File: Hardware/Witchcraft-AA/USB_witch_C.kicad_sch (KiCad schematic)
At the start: 11 parts, among them J0 USB_C_Molex_201267-0005, J1 USB_C_Molex_201267-0005, U1 Z1 extreme

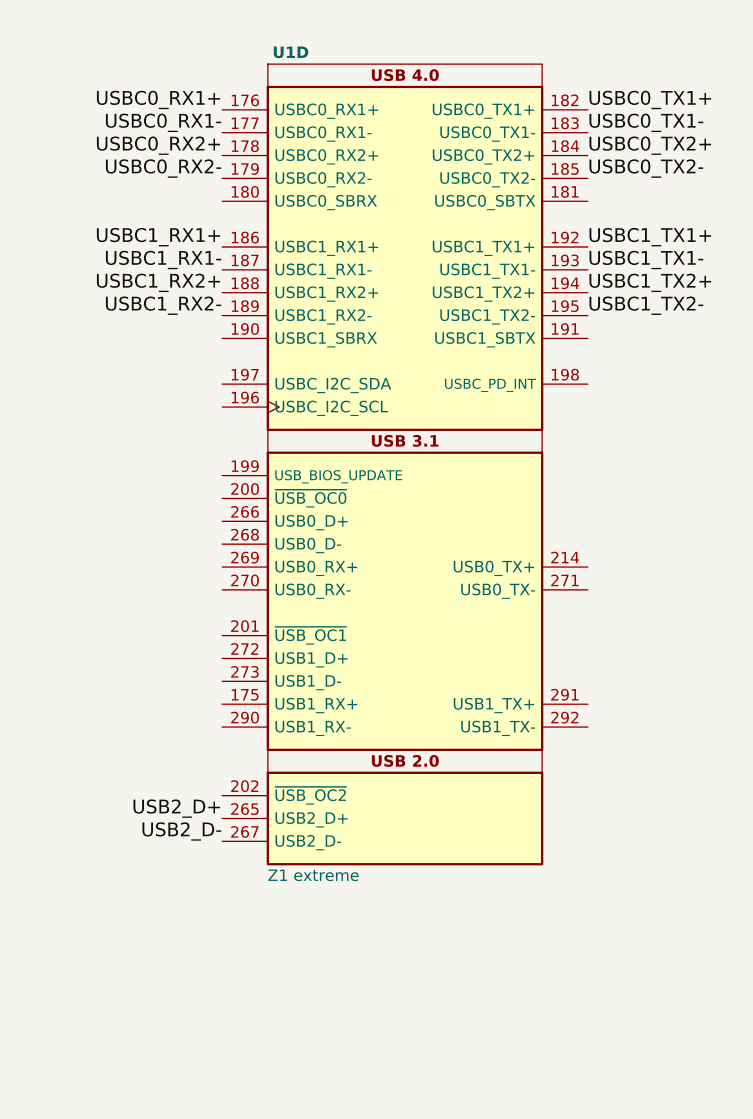
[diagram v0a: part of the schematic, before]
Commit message: ECAD: replaced the Z1 Extreme with the 7840U chip, as the AI-engine will be more useful for makers and non-gamers. MCAD: continued converting the outer shell towards a Assembly4-architecture, adding more items. Started a big change in design wherein I'm splitting the shell-design into a modular one, to accomodate removable controllers. Made some minor tweaks to the cooling-assembly, to accomodate the new, split shell-design. Updated the Readme to describe the project.
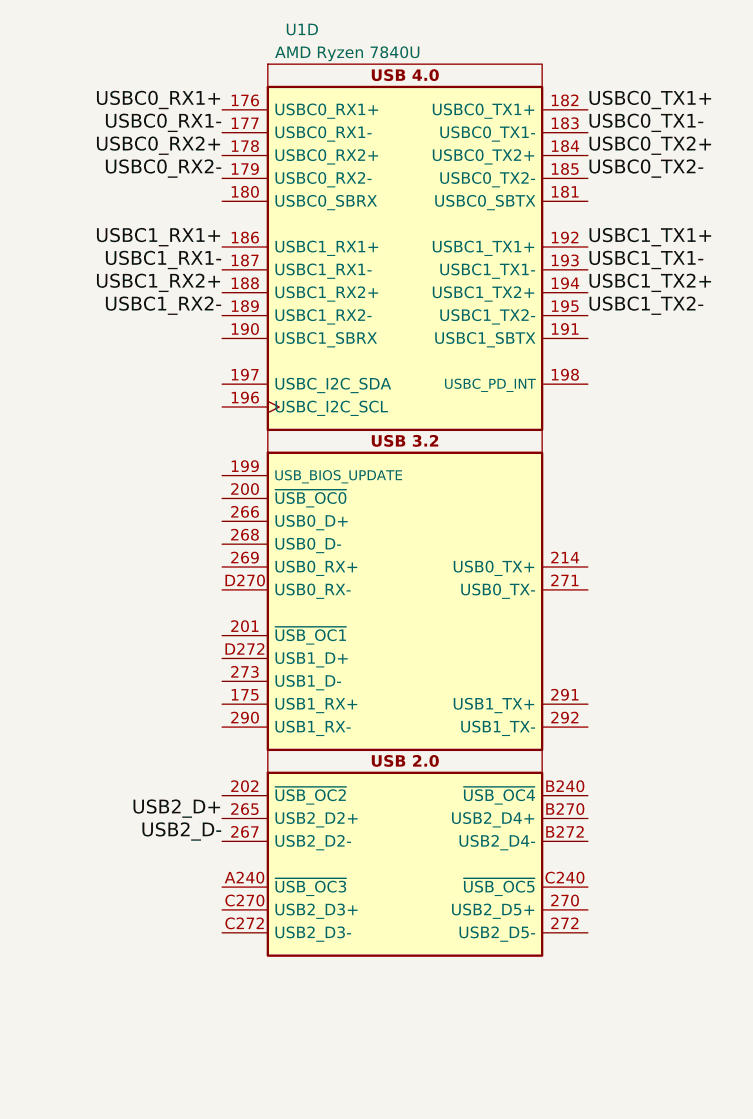
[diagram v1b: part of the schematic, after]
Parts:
- U1: value Z1 extreme -> AMD Ryzen 7840U; symbol LRJ-parts:AMD_Z1_extreme -> LRJ-parts:AMD_Ryzen_7840U_FP8; Details https://en.wikichip.org/wiki/amd/packages/socket_am5#Packag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 -> https://en.wikichip.org/wiki/amd/packages/fp6; Operating temperature (none) -> 0 C ~ 45 C
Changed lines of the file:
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@@
     )
   )
-  (symbol (lib_id "LRJ-parts:AMD_Z1_extreme") (at 321.31 71.12 0) (unit 4)
+  (symbol (lib_id "LRJ-parts:AMD_Ryzen_7840U_FP8") (at 321.31 71.12 0) (unit 4)
     (in_bom yes) (on_board yes) (dnp no)
-    (property "Reference" "U1" (at 308.61 26.67 0)
-      (effects (font (size 1.27 1.27) bold))
-    )
-    (property "Value" "Z1 extreme" (at 311.15 118.11 0)
+    (property "Reference" "U1" (at 309.88 24.13 0)
       (effects (font (size 1.27 1.27)))
     )
-    (property "Footprint" "LRJ:Package_BGA_FP8" (at 468.63 43.18 0)
+    (property "Value" "AMD Ryzen 7840U" (at 314.96 26.67 0)
+      (effects (font (size 1.27 1.27)))
+    )
+    (property "Footprint" "LRJ:Package_BGA_FP8" (at 343.535 -25.4 0)
       (effects (font (size 1.27 1.27)) hide)
     )
-    (property "Datasheet" "" (at 468.63 43.18 0)
+    (property "Datasheet" "" (at 344.17 -22.86 0)
       (effects (font (size 1.27 1.27)) hide)
     )
-    (property "Manufacturer" "Advanced Micro Devices" (at 340.36 -12.7 0)
+    (property "Manufacturer" "Advanced Micro Devices" (at 344.17 -33.02 0)
       (effects (font (size 1.27 1.27)) hide)
     )
-    (property "MPN" "100-000001131" (at 331.47 -10.16 0)
+    (property "MPN" "100-000001131" (at 340.995 -30.48 0)
       (effects (font (size 1.27 1.27)) hide)
     )
-    (property "Details" "https://en.wikichip.org/wiki/amd/packages/socket_am5#Package_Diagrams" (at 367.665 -6.985 0)
+    (property "Details" "https://en.wikichip.org/wiki/amd/packages/fp6" (at 369.57 -27.94 0)
       (effects (font (size 1.27 1.27)) hide)
     )
-    (property "Sim.Enable" "0" (at 321.31 71.12 0)
+    (property "Sim.Enable" "0" (at 354.33 63.5 0)
+      (effects (font (size 1.27 1.27)) hide)
+    )
+    (property "Operating temperature" "0 C ~ 45 C" (at 359.41 68.58 0)
       (effects (font (size 1.27 1.27)) hide)
     )
@@
     (pin "23")
     (pin "24")
-    (pin "25")
-    (pin "25")
-    (pin "25")
-    (pin "25")
-    (pin "25")
-    (pin "25")
-    (pin "25")
-    (pin "25")
-    (pin "25")
-    (pin "25")
-    (pin "25")
-    (pin "25")
     (pin "26")
     (pin "27")
@@
     (pin "8")
     (pin "9")
+    (pin "A250")
     (pin "AK1")
     (pin "AP3")
@@
     (pin "AY1")
     (pin "AY4")
+    (pin "B250")
     (pin "BA5")
     (pin "BB3")
+    (pin "C250")
+    (pin "D250")
+    (pin "E250")
+    (pin "F250")
+    (pin "G250")
+    (pin "H250")
+    (pin "I250")
+    (pin "J250")
+    (pin "K250")
+    (pin "L250")
     (pin "100")
     (pin "101")
@@
     (pin "98")
     (pin "99")
-    (pin "111")
-    (pin "112")
     (pin "114")
     (pin "123")
@@
     (pin "288")
     (pin "289")
-    (pin "47")
-    (pin "48")
     (pin "51")
+    (pin "A11")
+    (pin "A112")
+    (pin "A47")
+    (pin "A48")
     (pin "175")
     (pin "176")
@@
     (pin "291")
     (pin "292")
+    (pin "A240")
+    (pin "B240")
+    (pin "B270")
+    (pin "B272")
+    (pin "C240")
+    (pin "C270")
+    (pin "C272")
+    (pin "D270")
+    (pin "D272")
     (pin "203")
     (pin "204")
@@
     (pin "210")
     (pin "211")
-    (pin "211")
     (pin "215")
     (pin "216")
     (pin "217")
-    (pin "218")
     (pin "218")
     (pin "219")
@@
     (pin "310")
     (pin "311")
+    (pin "A211")
+    (pin "A218")
     (pin "BB20")
     (pin "BB5")
@@
     (pin "254")
     (pin "32")
-    (pin "32")
     (pin "A10")
     (pin "A12")
-    (pin "A14")
     (pin "A16")
-    (pin "A19")
-    (pin "A21")
-    (pin "A23")
+    (pin "A190")
+    (pin "A210")
+    (pin "A230")
     (pin "A26")
-    (pin "A3")
     (pin "A30")
+    (pin "A302")
+    (pin "A32")
     (pin "A5")
     (pin "A7")
@@
     (pin "AY8")
     (pin "B28")
-    (pin "B28")
-    (pin "B28")
-    (pin "B28")
-    (pin "B28")
-    (pin "B28")
+    (pin "B280")
+    (pin "B281")
+    (pin "B282")
+    (pin "B283")
+    (pin "B284")
     (pin "BB1")
     (pin "BB32")
@@
     (pin "C10")
     (pin "C3")
-    (pin "C32")
+    (pin "D14")
     (pin "E10")
     (pin "E11")
@@
     (pin "E26")
     (pin "E27")
+    (pin "E32")
     (pin "E7")
     (pin "E8")
@@
     (pin "A20")
     (pin "A21")
-    (pin "A22")
+    (pin "A222")
     (pin "A23")
     (pin "A24")
@@
     (pin "A300")
     (pin "A31")
-    (pin "A32")
+    (pin "A323")
     (pin "A33")
     (pin "A34")
@@
     (pin "B26")
     (pin "B27")
-    (pin "B28")
+    (pin "B285")
     (pin "B29")
     (pin "B30")
@@
     (pin "D37")
     (pin "14")
-    (pin "14")
-    (pin "15")
-    (pin "15")
-    (pin "15")
     (pin "15")
     (pin "17")
@@
     (pin "20")
     (pin "A1")
-    (pin "A1")
-    (pin "A1")
-    (pin "A1")
-    (pin "A1")
-    (pin "A1")
-    (pin "A1")
-    (pin "A1")
-    (pin "A1")
-    (pin "A1")
-    (pin "A1")
-    (pin "A1")
-    (pin "A1")
+    (pin "A111")
+    (pin "A121")
+    (pin "A122")
+    (pin "A123")
+    (pin "A124")
+    (pin "A125")
+    (pin "A126")
+    (pin "A127")
+    (pin "A128")
+    (pin "A129")
+    (pin "A130")
+    (pin "A131")
     (pin "A14")
-    (pin "A14")
-    (pin "A14")
-    (pin "A2")
-    (pin "A2")
-    (pin "A2")
-    (pin "A2")
-    (pin "A2")
-    (pin "A2")
-    (pin "A2")
-    (pin "A2")
-    (pin "A2")
-    (pin "A2")
-    (pin "A2")
-    (pin "A2")
-    (pin "A2")
+    (pin "A140")
+    (pin "A150")
+    (pin "A220")
+    (pin "A221")
     (pin "A3")
-    (pin "A3")
+    (pin "A301")
     (pin "A4")
-    (pin "A4")
-    (pin "A5")
+    (pin "A401")
+    (pin "A501")
     (pin "A6")
     (pin "A8")
-    (pin "A8")
-    (pin "A8")
+    (pin "A801")
+    (pin "A802")
+    (pin "B14")
+    (pin "B150")
+    (pin "B2")
+    (pin "C14")
+    (pin "C150")
+    (pin "C2")
+    (pin "D2")
+    (pin "E2")
+    (pin "F2")
+    (pin "G2")
+    (pin "H2")
+    (pin "I2")
+    (pin "J2")
+    (pin "K2")
+    (pin "L2")
     (pin "10")
     (pin "11")

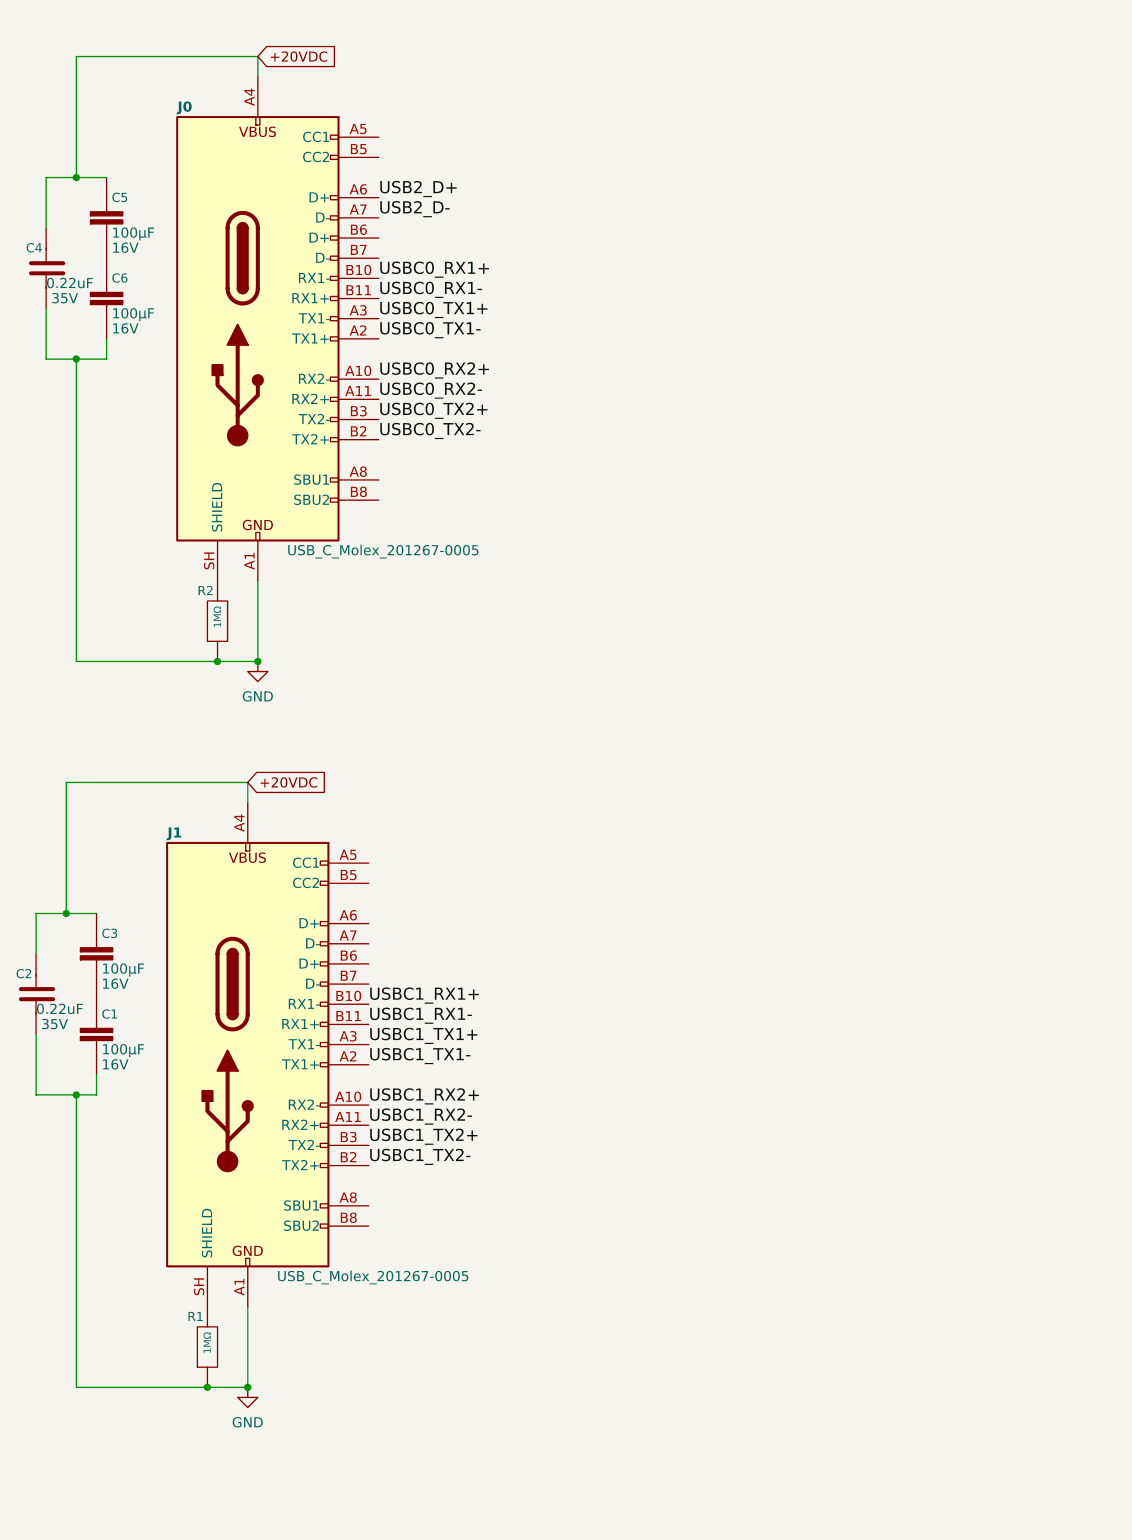
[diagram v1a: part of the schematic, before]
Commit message: MCAD: Added Oculink connector. ECAD: Added Oculink connector.
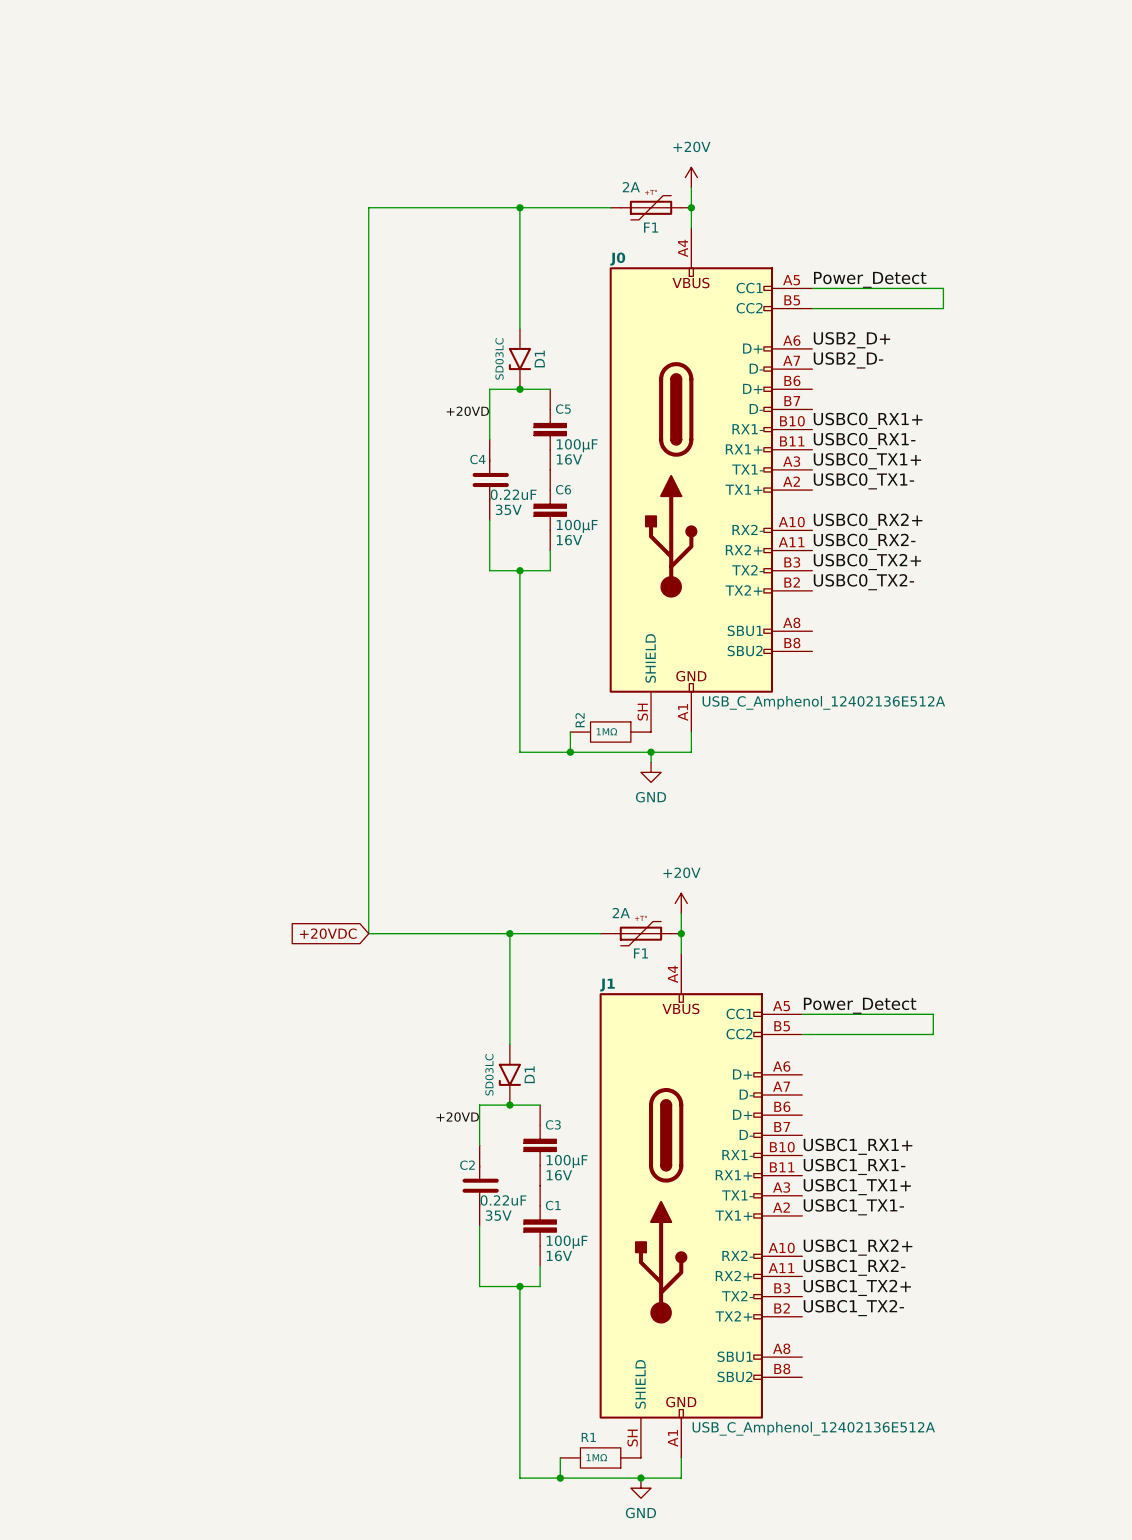
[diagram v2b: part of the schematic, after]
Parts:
- added D1 (x2): SD03LC, Diode_SMD:D_SOD-323, symbol LRJ-parts:D_SD03LC
- added F1 (x2): PPTC_SMD2920B200, LRJ:Fuse_Yageo_SMD2920B200TF_L7.3mm_W5.1mm, symbol LRJ-parts:PPTC_SMD2920B200
- J0, J1: value USB_C_Molex_201267-0005 -> USB_C_Amphenol_12402136E512A; footprint LRJ:USB-C_Receptacle_2012670005 -> LRJ:USB-C_Receptacle_Amphenol_12402136E512A; symbol LRJ-parts:USB_C_Molex_201267-0005 -> LRJ-parts:USB_C_Amphenol_12402136E512A; Detail page (none) -> https://www.amphenol-cs.com/usb4-gen3-type-c-12402136e512a.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; MPN 201267-0005 -> 12402136E512A; Manufacturer Molex -> Amphenol ICC; Status (none) -> Active; Voltage rating 30V -> 20V
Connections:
- net +20VDC: now also D1.2 (A2), D1.2 (A2), F1.1, F1.1; no longer C2.1, C3.1, C4.1, C5.1, J0.A4 (VBUS), J0.A9 (VBUS), J0.B4 (VBUS), J0.B9 (VBUS), J1.A4 (VBUS), J1.A9 (VBUS), J1.B4 (VBUS), J1.B9 (VBUS)
- net GND: now also R1.2, R2.2; no longer R1.1, R2.1
- net Power_Detect: now reaches J1.A5 (CC1)
- net Power_Detect: now also J0.A5 (CC1), J0.B5 (CC2), J1.B5 (CC2)
- net at J1.SH (SHIELD): now also R1.1; no longer R1.2
- net at J0.SH (SHIELD): now also R2.1; no longer R2.2
- new net +20V: F1.2, F1.2, J0.A4 (VBUS), J0.A9 (VBUS), J0.B4 (VBUS), J0.B9 (VBUS), J1.A4 (VBUS), J1.A9 (VBUS), J1.B4 (VBUS), J1.B9 (VBUS)
- new net +20VD: C2.1, C3.1, C4.1, C5.1, D1.1 (A1), D1.1 (A1)
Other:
- title: (none) -> WITCHCRAFT HANDHELD
- moved on the sheet: C1, C2, C3, C4, C5, C6, J0, J1
